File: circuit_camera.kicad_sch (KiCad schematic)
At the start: 0 parts

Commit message: Je sais plus
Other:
- company: (none) -> GAUL
- title: (none) -> Payload
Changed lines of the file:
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@@
 (kicad_sch (version 20230121) (generator eeschema)
   (paper "A4")
+  (title_block
+    (title "Payload")
+    (rev "0")
+    (company "GAUL")
+  )
 )

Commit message: Ajout page Vbuck
Le régulateur de tension buck converter a été ajouté au payload dans la page Vbuck qui remplace la page circuit caméras.
J'ai enlevé la switch du buck et connecté l'entré on/off à GND.
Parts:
- added Cin1: 100u, Capacitor_THT:CP_Radial_D8.0mm_P3.50mm, symbol Device:C
- added Cout1: 1000u, Capacitor_THT:CP_Radial_D10.0mm_P5.00mm, symbol Device:C
- added D1: 1N5820, Diode_THT:D_DO-201AD_P15.24mm_Horizontal, symbol Diode:1N5820
- added D2: LED, GAUL-Empreintes:LED_classique_TH, symbol Device:LED
- added H1, H2, H3, H4: ~, GAUL-Empreintes:Ground_mounting_hole_1mm, symbol GAUL-Symboles:Ground_mounting_hole_1mm
- added Lout1: 100u, LM2576:IND_YUDEN_NS12575_YDN, symbol Device:L
- added R7: R, GAUL-Empreintes:Resistance_TH_classique, symbol Device:R
- added U11: LM2576HVS-5, Package_TO_SOT_SMD:TO-263-5_TabPin3, symbol Regulator_Switching:LM2576HVS-5
- added bornier1: Conn_batterie, symbol GAUL-Symboles:Conn_batterie
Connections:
- new net: Cin1.1, U11.1 (VIN), bornier1.1 (Vbatterie)
- new net: D1.1 (K), Lout1.1, U11.2 (OUT)
- new net: D2.1 (-), R7.1
- new net +3.3V: Cout1.1, D2.2 (+), Lout1.2, U11.4 (FB)
- new net GND: Cin1.2, Cout1.2, D1.2 (A), H1.1, H2.1, H3.1, H4.1, R7.2, U11.3 (GND), U11.5 (~{ON}/OFF), bornier1.0 (GND)

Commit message: Revert "Recommit du Vbuck"
This reverts commit db6b1385e92bec759ec8c6f30127fdc08b8b4918.
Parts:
- removed Cin1: 100u, Capacitor_THT:CP_Radial_D8.0mm_P3.50mm, symbol Device:C
- removed Cout1: 1000u, Capacitor_THT:CP_Radial_D10.0mm_P5.00mm, symbol Device:C
- removed D1: 1N5820, Diode_THT:D_DO-201AD_P15.24mm_Horizontal, symbol Diode:1N5820
- removed D2: LED, GAUL-Empreintes:LED_classique_TH, symbol Device:LED
- removed H1, H2, H3, H4: ~, GAUL-Empreintes:Ground_mounting_hole_1mm, symbol GAUL-Symboles:Ground_mounting_hole_1mm
- removed Lout1: 100u, LM2576:IND_YUDEN_NS12575_YDN, symbol Device:L
- removed R7: R, GAUL-Empreintes:Resistance_TH_classique, symbol Device:R
- removed U11: LM2576HVS-5, Package_TO_SOT_SMD:TO-263-5_TabPin3, symbol Regulator_Switching:LM2576HVS-5
- removed bornier1: Conn_batterie, symbol GAUL-Symboles:Conn_batterie

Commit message: Re-re-buck
J'ai pris les trucs à Vincent et refait les modifs du buck converter.
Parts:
- added Cin1: 100u, Capacitor_THT:CP_Radial_D8.0mm_P3.50mm, symbol Device:C
- added Cout1: 1000u, Capacitor_THT:CP_Radial_D10.0mm_P5.00mm, symbol Device:C
- added D1: 1N5820, Diode_THT:D_DO-201AD_P15.24mm_Horizontal, symbol Diode:1N5820
- added D2: LED, GAUL-Empreintes:LED_classique_TH, symbol Device:LED
- added H1, H2, H3, H4: ~, GAUL-Empreintes:Ground_mounting_hole_1mm, symbol GAUL-Symboles:Ground_mounting_hole_1mm
- added Lout1: 100u, LM2576:IND_YUDEN_NS12575_YDN, symbol Device:L
- added R7: R, GAUL-Empreintes:Resistance_TH_classique, symbol Device:R
- added U11: LM2576HVS-5, Package_TO_SOT_SMD:TO-263-5_TabPin3, symbol Regulator_Switching:LM2576HVS-5
- added bornier1: Conn_batterie, symbol GAUL-Symboles:Conn_batterie
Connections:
- new net: D2.1 (-), R7.1
- new net: Cin1.1, U11.1 (VIN), bornier1.1 (Vbatterie)
- new net: D1.1 (K), Lout1.1, U11.2 (OUT)
- new net +3.3V: Cout1.1, D2.2 (+), Lout1.2, U11.4 (FB)
- new net GND: Cin1.2, Cout1.2, D1.2 (A), H1.1, H2.1, H3.1, H4.1, R7.2, U11.3 (GND), U11.5 (~{ON}/OFF), bornier1.0 (GND)

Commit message: Plein de modifs
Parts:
- added C1LDO, C2LDO: 10u, symbol Device:C_Small
- added D3, D4: D_Schottky, symbol Device:D_Schottky
- added F1, F2: Fuse, symbol Device:Fuse
- added FB1: FerriteBead, symbol Device:FerriteBead
- added U12: LDO 5-3.3V-(MIC5504-3.3YM5-TR), SOT-23-5_MC_MCH, symbol GAUL-Symboles:LDO 5-3.3V-(MIC5504-3.3YM5-TR)
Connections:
- net +3.3V: now also C2LDO.1, U12.5 (VOUT)
- net GND: now also C1LDO.2, C2LDO.2, U12.2 (GND)
- net at Cin1.1, U11.1 (VIN): now also D3.1 (K), D3.2 (A), F2.2; no longer bornier1.1 (Vbatterie)
- new net: F2.1, bornier1.1 (Vbatterie)
- new net: D4.1 (K), FB1.1
- new net: C1LDO.1, FB1.2, U12.1 (VIN)
- new net: D4.2 (A), F1.2
- new net Vusb: F1.1, U12.3 (EN)
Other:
- moved on the sheet: bornier1

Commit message: Mémoire
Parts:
- added R33: 33k, GAUL-Empreintes:Resistance_TH_classique, symbol Device:R
- added R34: R, GAUL-Empreintes:Resistance_TH_classique, symbol Device:R
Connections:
- net GND: now also R34.2
- net Vusb: now also R33.1
- new net USB_check: R33.2, R34.1
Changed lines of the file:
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@@
   (junction (at 127 107.95) (diameter 0) (color 0 0 0 0)
   )
+  (junction (at 77.47 139.7) (diameter 0) (color 0 0 0 0)
+  )
   (junction (at 189.23 91.44) (diameter 0) (color 0 0 0 0)
   )
@@
     (stroke (width 0) (type default))
   )
+  (wire (pts (xy 71.12 139.7) (xy 77.47 139.7))
+    (stroke (width 0) (type default))
+  )
+  (wire (pts (xy 77.47 151.13) (xy 77.47 148.59))
+    (stroke (width 0) (type default))
+  )
   (wire (pts (xy 173.99 91.44) (xy 189.23 91.44))
     (stroke (width 0) (type default))
@@
     (stroke (width 0) (type default))
   )
-  (wire (pts (xy 82.55 139.7) (xy 85.09 139.7))
-    (stroke (width 0) (type default))
-  )
   (wire (pts (xy 105.41 86.36) (xy 107.95 86.36))
     (stroke (width 0) (type default))
@@
     (stroke (width 0) (type default))
   )
+  (wire (pts (xy 77.47 139.7) (xy 85.09 139.7))
+    (stroke (width 0) (type default))
+  )
   (wire (pts (xy 127 69.85) (xy 127 67.31))
     (stroke (width 0) (type default))
@@
   )
   (wire (pts (xy 127 91.44) (xy 132.08 91.44))
+    (stroke (width 0) (type default))
+  )
+  (wire (pts (xy 77.47 140.97) (xy 77.47 139.7))
     (stroke (width 0) (type default))
   )
@@
     )
   )
-  (global_label "Vusb" (shape input) (at 82.55 139.7 180) (fields_autoplaced)
+  (global_label "Vusb" (shape input) (at 71.12 139.7 180) (fields_autoplaced)
     (effects (font (size 1.27 1.27)) (justify right))
-    (property "Intersheetrefs" "${INTERSHEET_REFS}" (at 75.1501 139.7 0)
+    (property "Intersheetrefs" "${INTERSHEET_REFS}" (at 63.7201 139.7 0)
       (effects (font (size 1.27 1.27)) (justify right) hide)
+    )
+  )
+  (global_label "USB_check" (shape input) (at 77.47 149.86 0) (fields_autoplaced)
+    (effects (font (size 1.27 1.27)) (justify left))
+    (property "Intersheetrefs" "${INTERSHEET_REFS}" (at 90.6757 149.86 0)
+      (effects (font (size 1.27 1.27)) (justify left) hide)
     )
   )
@@
     )
   )
+  (symbol (lib_id "Device:R") (at 77.47 144.78 0) (unit 1)
+    (in_bom yes) (on_board yes) (dnp no)
+    (property "Reference" "R33" (at 72.39 142.24 0)
+      (effects (font (size 1.27 1.27)) (justify left))
+    )
+    (property "Value" "33k" (at 73.66 144.78 0)
+      (effects (font (size 1.27 1.27)) (justify left))
+    )
+    (property "Footprint" "GAUL-Empreintes:Resistance_TH_classique" (at 75.692 144.78 90)
+      (effects (font (size 1.27 1.27)) hide)
+    )
+    (property "Datasheet" "~" (at 77.47 144.78 0)
+      (effects (font (size 1.27 1.27)) hide)
+    )
+    (pin "1")
+    (pin "2")
+    (instances
+      (project "Payload"
+        (path "/5f62c44b-34ee-4720-b187-b4a520863a8a/b731aecd-8fa5-4432-90a5-bb6d0ae39f62"
+          (reference "R33") (unit 1)
+        )
+      )
+      (project "Buck_5V"
+        (path "/b57e233b-724e-41fe-b467-3bde33ee5ca1"
+          (reference "R1") (unit 1)
+        )
+      )
+    )
+  )
   (symbol (lib_id "power:GND") (at 142.24 69.85 0) (unit 1)
     (in_bom yes) (on_board yes) (dnp no) (fields_autoplaced)
@@
     )
   )
+  (symbol (lib_id "Device:R") (at 77.47 154.94 0) (unit 1)
+    (in_bom yes) (on_board yes) (dnp no)
+    (property "Reference" "R34" (at 72.39 152.4 0)
+      (effects (font (size 1.27 1.27)) (justify left))
+    )
+    (property "Value" "R" (at 73.66 154.94 0)
+      (effects (font (size 1.27 1.27)) (justify left))
+    )
+    (property "Footprint" "GAUL-Empreintes:Resistance_TH_classique" (at 75.692 154.94 90)
+      (effects (font (size 1.27 1.27)) hide)
+    )
+    (property "Datasheet" "~" (at 77.47 154.94 0)
+      (effects (font (size 1.27 1.27)) hide)
+    )
+    (pin "1")
+    (pin "2")
+    (instances
+      (project "Payload"
+        (path "/5f62c44b-34ee-4720-b187-b4a520863a8a/b731aecd-8fa5-4432-90a5-bb6d0ae39f62"
+          (reference "R34") (unit 1)
+        )
+      )
+      (project "Buck_5V"
+        (path "/b57e233b-724e-41fe-b467-3bde33ee5ca1"
+          (reference "R1") (unit 1)
+        )
+      )
+    )
+  )
   (symbol (lib_id "power:GND") (at 194.31 107.95 0) (unit 1)
     (in_bom yes) (on_board yes) (dnp no) (fields_autoplaced)
@@
         )
       )
+    )
+  )
+  (symbol (lib_id "power:GND") (at 77.47 158.75 0) (unit 1)
+    (in_bom yes) (on_board yes) (dnp no) (fields_autoplaced)
+    (property "Reference" "#PWR031" (at 77.47 165.1 0)
+      (effects (font (size 1.27 1.27)) hide)
+    )
+    (property "Value" "GND" (at 77.47 163.83 0)
+      (effects (font (size 1.27 1.27)))
+    )
+    (property "Footprint" "" (at 77.47 158.75 0)
+      (effects (font (size 1.27 1.27)) hide)
+    )
+    (property "Datasheet" "" (at 77.47 158.75 0)
+      (effects (font (size 1.27 1.27)) hide)
+    )
+    (pin "1")
+    (instances
+      (project "Payload"
+        (path "/5f62c44b-34ee-4720-b187-b4a520863a8a/b731aecd-8fa5-4432-90a5-bb6d0ae39f62"
+          (reference "#PWR031") (unit 1)
+        )
+      )

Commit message: Schematic fini, en théorie
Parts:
- removed F1, F2: Fuse, symbol Device:Fuse
- added C1LDO1, C2LDO1: 1u, symbol Device:C_Small
- added F3, F4: PTC_resettable_fuse_(MF-MSMF030-2), MF-MSMF030-2:FUSER_MF-MSMF030-2, symbol GAUL-Symboles:PTC_resettable_fuse_(MF-MSMF030-2)
- added U4: LDO_5-1.8V-(MIC5504-1.8YM5-TR), SOT-23-5_MC_MCH, symbol GAUL-Symboles:LDO_5-1.8V-(MIC5504-1.8YM5-TR)
- C1LDO, C2LDO: value 10u -> 1u
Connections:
- net +3.3V: now also C1LDO1.1, U4.1 (VIN), U4.3 (EN)
- net GND: now also C1LDO1.2, C2LDO1.2, U4.2 (GND)
- net Vusb: now also F4.1; no longer R33.1
- net at bornier1.1 (Vbatterie): now also F3.1
- net at C1LDO.1, FB1.2, U12.1 (VIN): now also R33.1
- net at Cin1.1, D3.1 (K), U11.1 (VIN): no longer D3.2 (A)
- net at D4.2 (A): now also F4.2
- new net: D3.2 (A), F3.2
- new net +1V8: C2LDO1.1, U4.5 (VOUT)
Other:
- note added: "7-40V"
- note added: "Puissance du Buck: Iload = 0.5A 0.5A x 3.3V = 1.65W à l'entré: 2W 2W/9V = 0.2222 A max On peut donc limiter la fuse à 0.5 A"
- moved on the sheet: C1LDO, C2LDO, D4, FB1, R33, R34, U12, bornier1

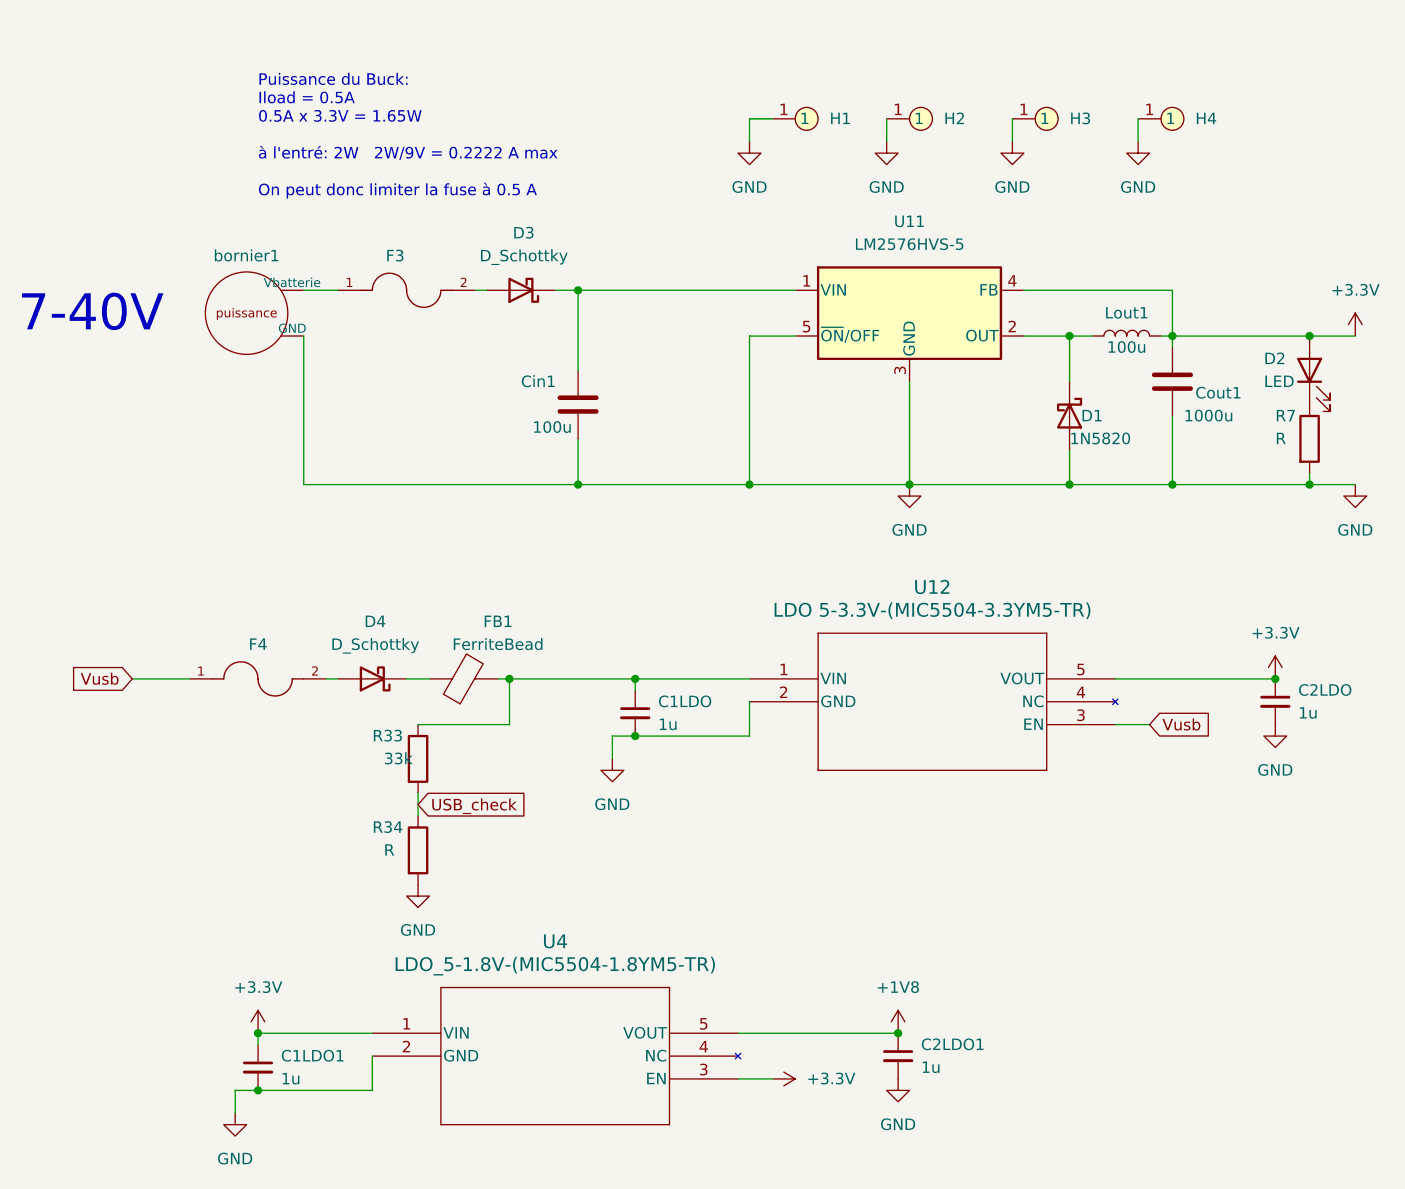
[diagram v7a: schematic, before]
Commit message: Petites modif et assignation des empreintes à 50%
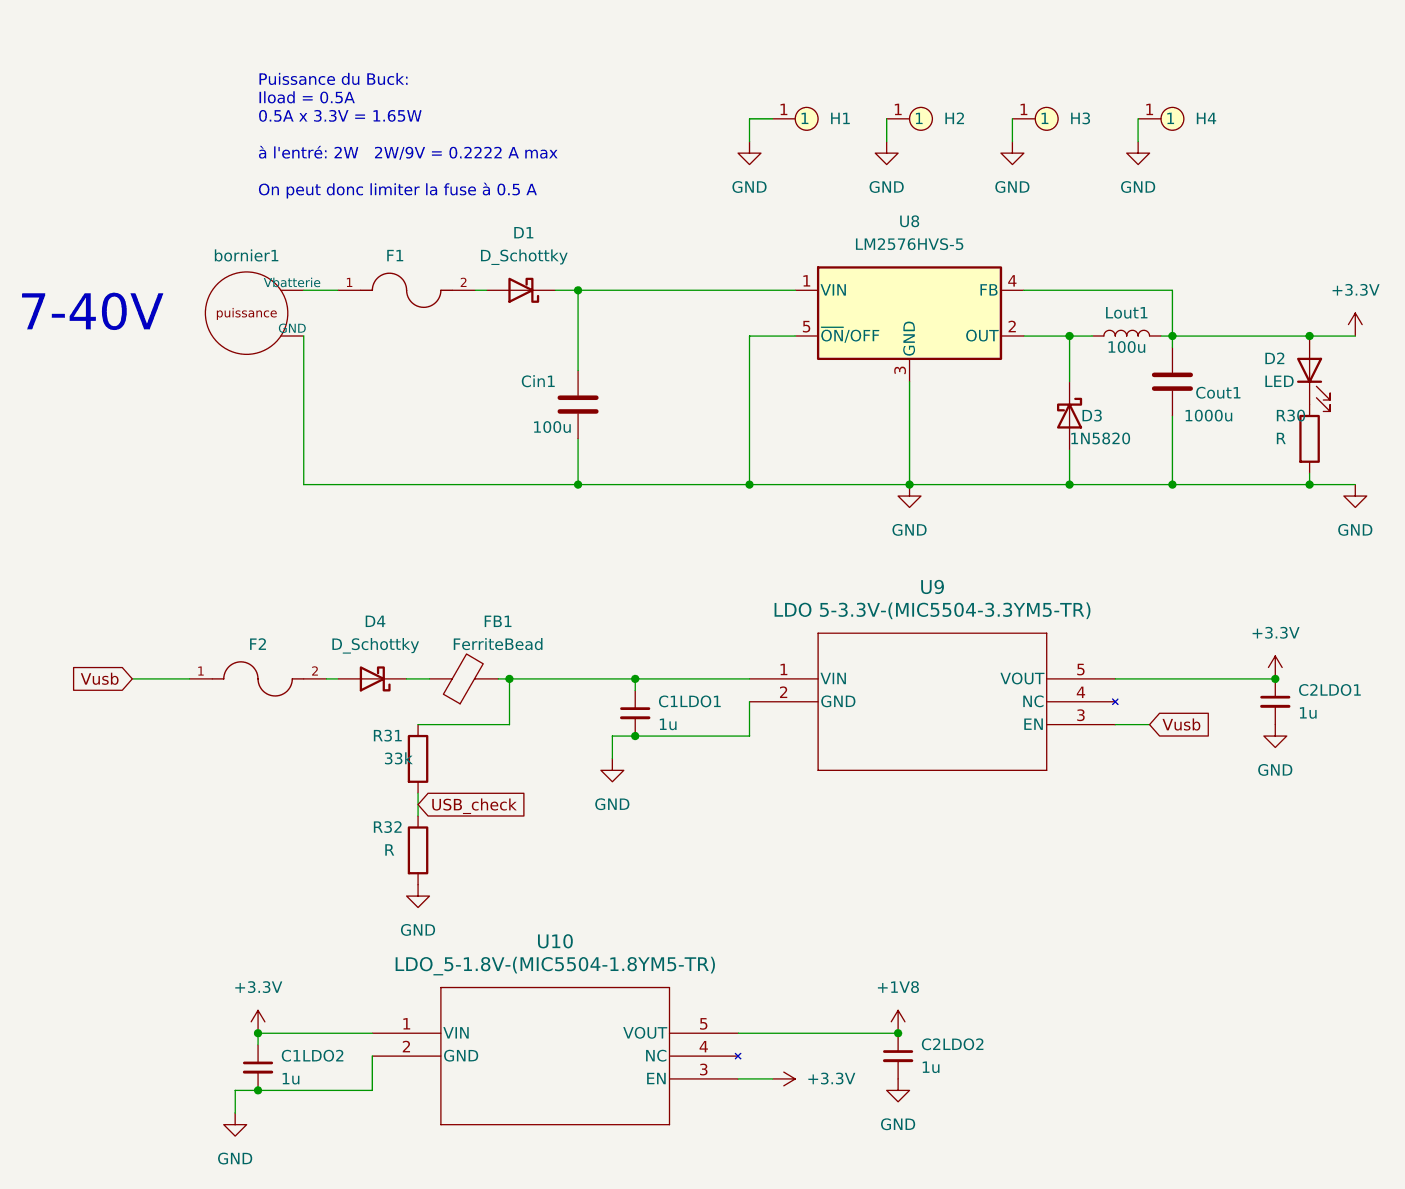
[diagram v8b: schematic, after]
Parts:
- C1LDO1: renamed from C1LDO; footprint (none) -> GAUL-Empreintes:cap-1uF-(CAPC0603X35N)
- C1LDO2: renamed from C1LDO1; footprint (none) -> GAUL-Empreintes:cap-1uF-(CAPC0603X35N)
- C2LDO1: renamed from C2LDO; footprint (none) -> GAUL-Empreintes:cap-1uF-(CAPC0603X35N)
- C2LDO2: renamed from C2LDO1; footprint (none) -> GAUL-Empreintes:cap-1uF-(CAPC0603X35N)
- U10: renamed from U4; footprint SOT-23-5_MC_MCH -> GAUL-Empreintes:SOT-23-5_MC_MCH
- U9: renamed from U12; footprint SOT-23-5_MC_MCH -> GAUL-Empreintes:SOT-23-5_MC_MCH
- bornier1: footprint (none) -> GAUL-Empreintes:Conn_batt_AWG14
- renumbered D3 to D1, D1 to D3, F3 to F1, F4 to F2, R7 to R30, R33 to R31, R34 to R32, U11 to U8
